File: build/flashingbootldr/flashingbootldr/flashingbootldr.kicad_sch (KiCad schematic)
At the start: 3 parts, among them U1 ATmega328P-P

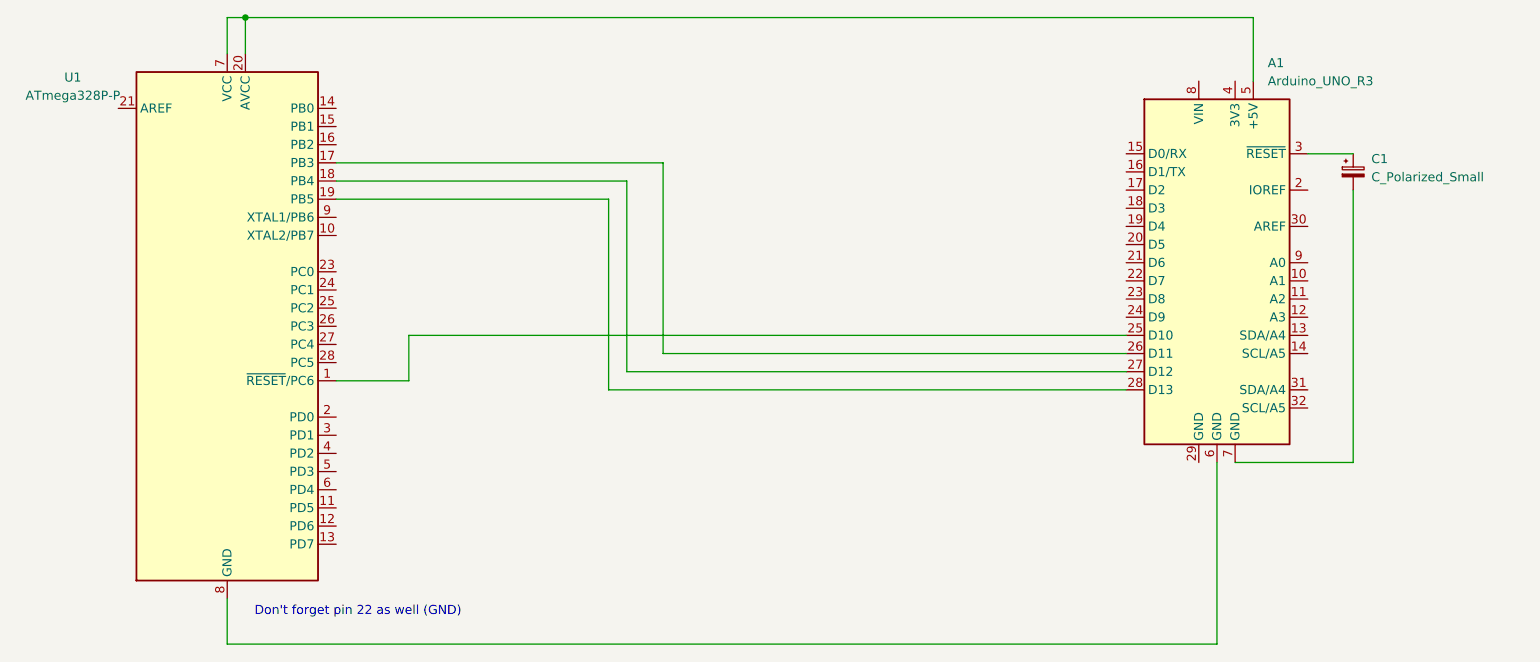
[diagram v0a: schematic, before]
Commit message: Fine tune edge cut
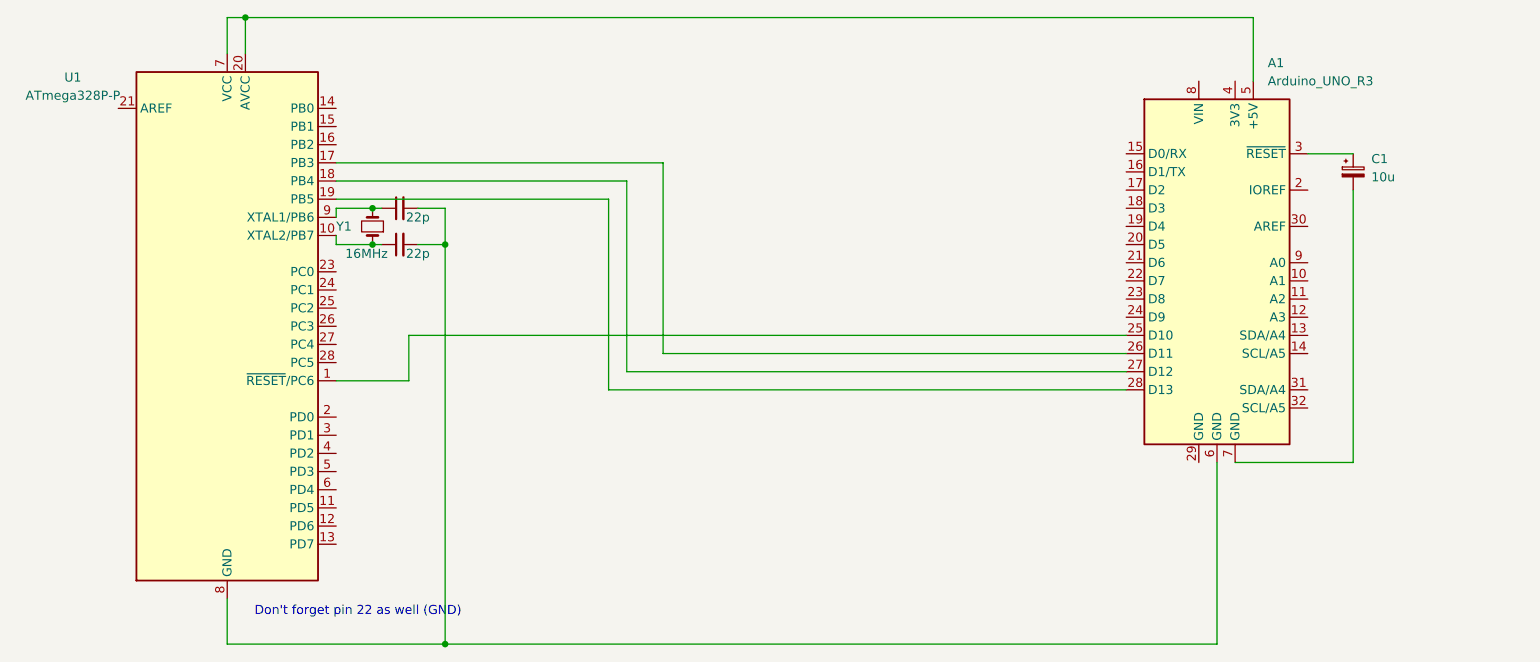
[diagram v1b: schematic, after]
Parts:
- added C1, C2: 22p, BlueJay footprints:C_Disc_D3.0mm_W1.6mm_P2.50mm, symbol BlueJaySymbolLibrary:C_Small
- added Y1: 16MHz, BlueJay footprints:Crystal_HC49-4H_Vertical, symbol BlueJaySymbolLibrary:Device_Crystal_Small
- C1: value C_Polarized_Small -> 10u
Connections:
- net at U1.10 (XTAL2/PB7): now also C2.1, Y1.1
- net at A1.6 (GND), U1.22 (GND), U1.8 (GND): now also C1.2, C2.2
- net at U1.9 (XTAL1/PB6): now also C1.1, Y1.2
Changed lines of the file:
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@@
   (junction (at 85.09 54.61) (diameter 0) (color 0 0 0 0)
   )
+  (junction (at 102.87 81.28) (diameter 0) (color 0 0 0 0)
+  )
+  (junction (at 113.03 86.36) (diameter 0) (color 0 0 0 0)
+  )
+  (junction (at 102.87 86.36) (diameter 0) (color 0 0 0 0)
+  )
+  (junction (at 113.03 142.24) (diameter 0) (color 0 0 0 0)
+  )
+  (wire (pts (xy 109.22 86.36) (xy 113.03 86.36))
+    (stroke (width 0) (type default) (color 0 0 0 0))
+  )
+  (wire (pts (xy 113.03 81.28) (xy 113.03 86.36))
+    (stroke (width 0) (type default) (color 0 0 0 0))
+  )
+  (wire (pts (xy 109.22 81.28) (xy 113.03 81.28))
+    (stroke (width 0) (type default) (color 0 0 0 0))
+  )
   (wire (pts (xy 85.09 54.61) (xy 85.09 59.69))
     (stroke (width 0) (type default) (color 0 0 0 0))
@@
     (stroke (width 0) (type default) (color 0 0 0 0))
   )
+  (wire (pts (xy 102.87 81.28) (xy 104.14 81.28))
+    (stroke (width 0) (type default) (color 0 0 0 0))
+  )
+  (wire (pts (xy 97.79 81.28) (xy 97.79 82.55))
+    (stroke (width 0) (type default) (color 0 0 0 0))
+  )
+  (wire (pts (xy 102.87 86.36) (xy 104.14 86.36))
+    (stroke (width 0) (type default) (color 0 0 0 0))
+  )
+  (wire (pts (xy 102.87 81.28) (xy 97.79 81.28))
+    (stroke (width 0) (type default) (color 0 0 0 0))
+  )
   (wire (pts (xy 220.98 116.84) (xy 220.98 142.24))
     (stroke (width 0) (type default) (color 0 0 0 0))
@@
     (stroke (width 0) (type default) (color 0 0 0 0))
   )
+  (wire (pts (xy 102.87 86.36) (xy 97.79 86.36))
+    (stroke (width 0) (type default) (color 0 0 0 0))
+  )
   (wire (pts (xy 240.03 116.84) (xy 223.52 116.84))
     (stroke (width 0) (type default) (color 0 0 0 0))
@@
     (stroke (width 0) (type default) (color 0 0 0 0))
   )
-  (wire (pts (xy 220.98 142.24) (xy 82.55 142.24))
+  (wire (pts (xy 220.98 142.24) (xy 113.03 142.24))
+    (stroke (width 0) (type default) (color 0 0 0 0))
+  )
+  (wire (pts (xy 113.03 142.24) (xy 82.55 142.24))
     (stroke (width 0) (type default) (color 0 0 0 0))
   )
@@
     (stroke (width 0) (type default) (color 0 0 0 0))
   )
+  (wire (pts (xy 97.79 86.36) (xy 97.79 85.09))
+    (stroke (width 0) (type default) (color 0 0 0 0))
+  )
   (wire (pts (xy 82.55 54.61) (xy 82.55 59.69))
     (stroke (width 0) (type default) (color 0 0 0 0))
@@
   )
   (wire (pts (xy 240.03 78.74) (xy 240.03 116.84))
+    (stroke (width 0) (type default) (color 0 0 0 0))
+  )
+  (wire (pts (xy 113.03 86.36) (xy 113.03 142.24))
     (stroke (width 0) (type default) (color 0 0 0 0))
   )
   (text "Don't forget pin 22 as well (GND)" (at 86.36 138.43 0)
     (effects (font (size 1.27 1.27)) (justify left bottom))
+  )
+  (symbol (lib_id "BlueJaySymbolLibrary:C_Small") (at 106.68 86.36 90) (unit 1)
+    (in_bom yes) (on_board yes)
+    (property "Reference" "C2" (id 0) (at 106.6863 80.01 90)
+      (effects (font (size 1.27 1.27)) hide)
+    )
+    (property "Value" "22p" (id 1) (at 109.22 87.63 90))
+    (property "Footprint" "BlueJay footprints:C_Disc_D3.0mm_W1.6mm_P2.50mm" (id 2) (at 106.68 86.36 0)
+      (effects (font (size 1.27 1.27)) hide)
+    )
+    (property "Datasheet" "~" (id 3) (at 106.68 86.36 0)
+      (effects (font (size 1.27 1.27)) hide)
+    )
+    (pin "1")
+    (pin "2")
+  )
+  (symbol (lib_id "BlueJaySymbolLibrary:C_Small") (at 106.68 81.28 90) (unit 1)
+    (in_bom yes) (on_board yes)
+    (property "Reference" "C1" (id 0) (at 106.6863 74.93 90)
+      (effects (font (size 1.27 1.27)) hide)
+    )
+    (property "Value" "22p" (id 1) (at 109.22 82.55 90))
+    (property "Footprint" "BlueJay footprints:C_Disc_D3.0mm_W1.6mm_P2.50mm" (id 2) (at 106.68 81.28 0)
+      (effects (font (size 1.27 1.27)) hide)
+    )
+    (property "Datasheet" "~" (id 3) (at 106.68 81.28 0)
+      (effects (font (size 1.27 1.27)) hide)
+    )
+    (pin "1")
+    (pin "2")
   )
   (symbol (lib_id "MCU_Microchip_ATmega:ATmega328P-P") (at 82.55 97.79 0) (unit 1)
@@
     (pin "8")
     (pin "9")
+  )
+  (symbol (lib_id "BlueJaySymbolLibrary:Device_Crystal_Small") (at 102.87 83.82 90) (unit 1)
+    (in_bom yes) (on_board yes)
+    (property "Reference" "Y1" (id 0) (at 97.79 83.82 90)
+      (effects (font (size 1.27 1.27)) (justify right))
+    )
+    (property "Value" "16MHz" (id 1) (at 99.06 87.63 90)
+      (effects (font (size 1.27 1.27)) (justify right))
+    )
+    (property "Footprint" "BlueJay footprints:Crystal_HC49-4H_Vertical" (id 2) (at 102.87 83.82 0)
+      (effects (font (size 1.27 1.27)) hide)
+    )
+    (property "Datasheet" "" (id 3) (at 102.87 83.82 0)
+      (effects (font (size 1.27 1.27)) hide)
+    )
+    (pin "1")
+    (pin "2")
   )
   (symbol (lib_id "MCU_Module:Arduino_UNO_R3") (at 220.98 88.9 0) (unit 1)
@@
       (effects (font (size 1.27 1.27)) (justify left))
     )
-    (property "Value" "C_Polarized_Small" (id 1) (at 242.57 76.9238 0)
+    (property "Value" "10u" (id 1) (at 242.57 76.9238 0)
       (effects (font (size 1.27 1.27)) (justify left))
     )
@@
       (reference "A1") (unit 1) (value "Arduino_UNO_R3") (footprint "Module:Arduino_UNO_R3")
     )
+    (path "/6e6cccbc-a74e-4e11-9b88-b67a3cff842f"
+      (reference "C1") (unit 1) (value "22p") (footprint "BlueJay footprints:C_Disc_D3.0mm_W1.6mm_P2.50mm")
+    )
     (path "/e158f13d-5c0b-45f6-891f-0ce1aff2290a"
-      (reference "C1") (unit 1) (value "C_Polarized_Small") (footprint "Capacitor_THT:CP_Radial_D5.0mm_P2.50mm")
+      (reference "C1") (unit 1) (value "10u") (footprint "Capacitor_THT:CP_Radial_D5.0mm_P2.50mm")
+    )
+    (path "/0850b3e6-8622-4222-b18c-368ddb71ef19"
+      (reference "C2") (unit 1) (value "22p") (footprint "BlueJay footprints:C_Disc_D3.0mm_W1.6mm_P2.50mm")
     )
     (path "/7c87ef67-9e40-4b3f-8eaf-78a4e3eed88d"
       (reference "U1") (unit 1) (value "ATmega328P-P") (footprint "Package_DIP:DIP-28_W7.62mm")
     )
-  )
+    (path "/ab690b00-c3af-49e1-b4e3-2a9abbf1b032"
+      (reference "Y1") (unit 1) (value "16MHz") (footprint "BlueJay footprints:Crystal_HC49-4H_Vertical")
+    )
+  )
